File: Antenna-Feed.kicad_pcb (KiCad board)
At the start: 2 copper layers, 74.9 x 97.5 mm, 19 parts, among them J1 Conn_01x01, J10 PC104PTH, J11 PC104PTH, J12 PC104PTH, J13 PC104PTH, J2 B3B-XH-A(LF)(SN), J3 SMA, J4 Conn_01x01, J5 Conn_01x01, J6 Conn_01x01, J7 Conn_01x01, J8 Conn_01x01, J9 B3B-XH-A(LF)(SN), SW1 LIMIT_SWITCH, SW2 LIMIT_SWITCH, U1 B3B-XH-A-AntennaFeed-DC(LF)(S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, U1 B3B-XH-A-AntennaFeed-DepPow(L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, U1 B3B-XH-A-AntennaFeed-RFDep(LF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, U1 NC7SZ157

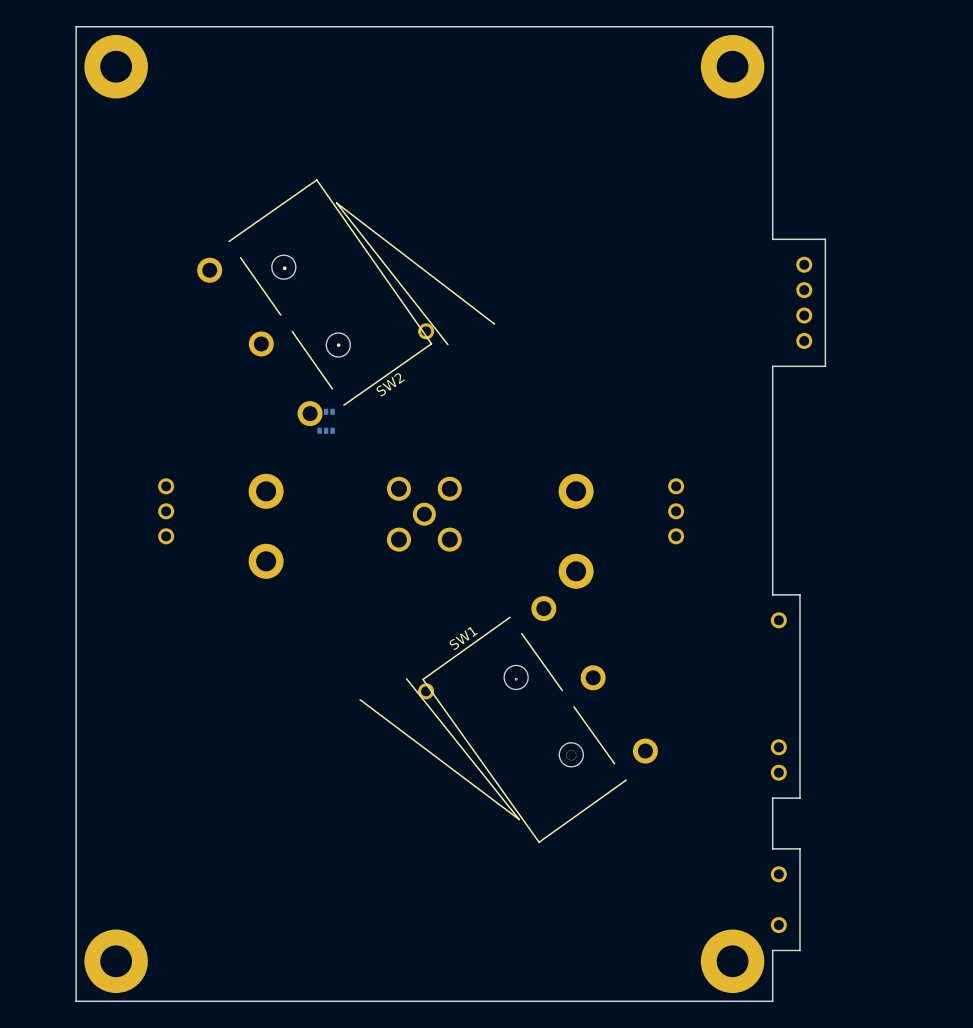
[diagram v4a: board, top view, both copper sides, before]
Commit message: fine tuned component placement
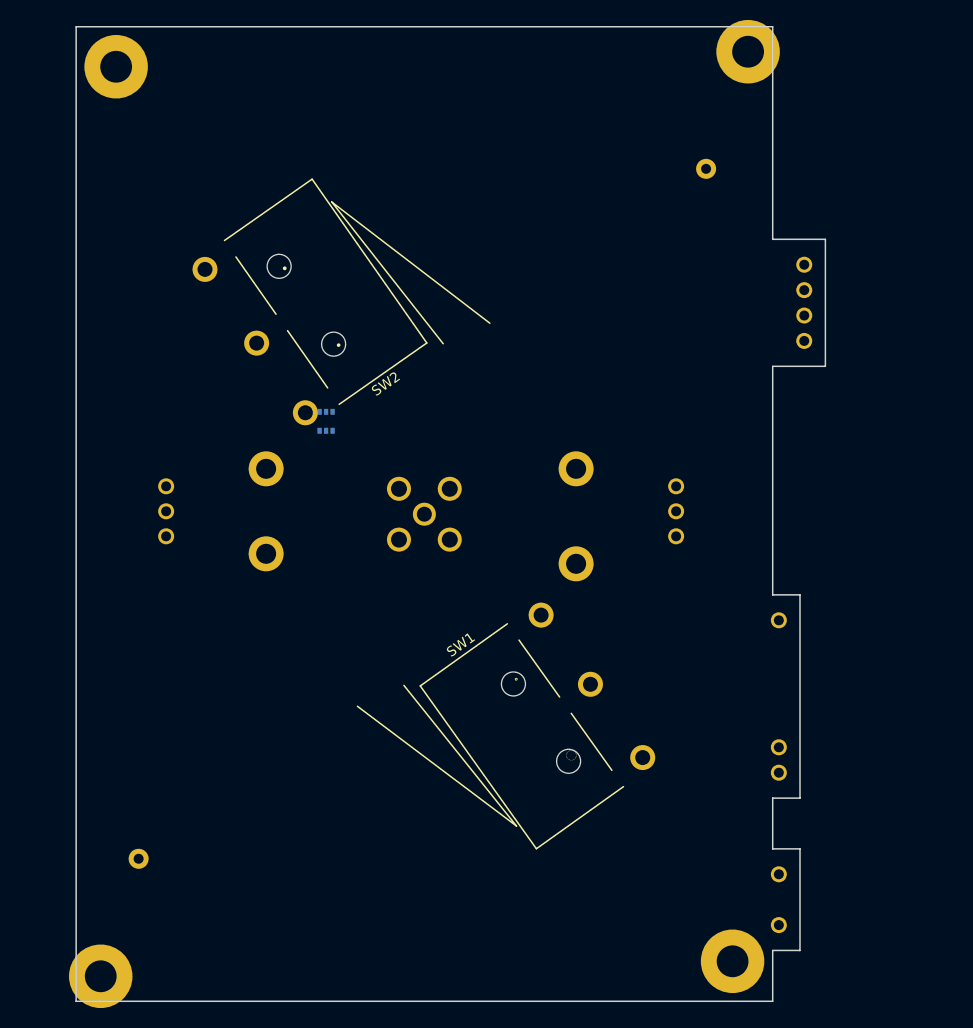
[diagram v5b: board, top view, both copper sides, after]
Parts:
- moved J1 33.3 mm to (96.2, 125.8)
- moved J4 32.4 mm to (153.0, 56.8)
- moved J6 2.25 mm to (109.0, 86.8)
- moved J8 2.25 mm to (140.0, 86.8)
- moved J13 2.16 mm to (157.2, 45.0)
- moved J11 2.15 mm to (92.5, 137.5)
- moved J5 0.75 mm to (109.0, 95.2)
- moved J7 0.75 mm to (140.0, 96.2)
- moved SW1 0.70 mm to (139.7, 109.8)
- moved SW2 0.48 mm to (109.7, 72.7)
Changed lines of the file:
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@@
     (links 17)
     (no_connects 17)
-    (area 89.924999 42.464999 165.005001 140.075001)
+    (area 80.650001 41.755 166.39 144.700001)
     (thickness 1.6)
     (drawings 22)
@@
     (add_net "Net-(J1-Pad1)")
   )
-  (module SFUSat:SMA-Vert-TH (layer B.Cu)
+  (module SFUSat:SMA-Vert-TH locked (layer B.Cu)
     (at 124.825 91.29)
     (fp_text reference J3 (at 0 -5.6) (layer B.SilkS)
@@
     )
   )
-  (module SFUSat:via-0.97mm (layer F.Cu)
-    (at 125 109)
-    (fp_text reference J1 (at 0.0635 2.032) (layer F.SilkS) hide
-      (effects (font (size 1 1) (thickness 0.15)))
-    )
-    (fp_text value Conn_01x01 (at 0.254 -2.8575) (layer F.Fab) hide
-      (effects (font (size 1 1) (thickness 0.15)))
-    )
-    (pad 1 thru_hole circle (at 0 0) (size 1.6 1.6) (drill 1) (layers *.Cu)
-      (net 1 "Net-(J1-Pad1)") (zone_connect 2))
-  )
-  (module SFUSat:via-0.97mm (layer F.Cu)
-    (at 125 73)
-    (fp_text reference J4 (at 0.0635 2.032) (layer F.SilkS) hide
-      (effects (font (size 1 1) (thickness 0.15)))
-    )
-    (fp_text value Conn_01x01 (at 0.254 -2.8575) (layer F.Fab) hide
-      (effects (font (size 1 1) (thickness 0.15)))
-    )
-    (pad 1 thru_hole circle (at 0 0) (size 1.6 1.6) (drill 1) (layers *.Cu)
-      (net 2 "Net-(J3-Pad2)") (zone_connect 2))
-  )
-  (module SFUSat:SS-3GLPD-R (layer F.Cu)
-    (at 140.02 109.16 125.5)
+  (module SFUSat:SS-3GLPD-R locked (layer F.Cu)
+    (at 139.748123 109.810139 125.5)
     (fp_text reference SW1 (at 11 -6 215.5) (layer F.SilkS)
       (effects (font (size 1 1) (thickness 0.15)))
@@
     )
   )
-  (module SFUSat:SS-3GLPD-R (layer F.Cu)
-    (at 110.218904 72.77 305)
+  (module SFUSat:SS-3GLPD-R locked (layer F.Cu)
+    (at 109.748904 72.685278 305)
     (fp_text reference SW2 (at 11 -6 395) (layer F.SilkS)
       (effects (font (size 1 1) (thickness 0.15)))
@@
       (net 8 "Net-(J10-Pad1)"))
   )
-  (module SFUSat:PC104PTH (layer F.Cu)
-    (at 94 136)
+  (module SFUSat:PC104PTH locked (layer F.Cu)
+    (at 92.46 137.5)
     (fp_text reference J11 (at 0 5.08) (layer F.SilkS) hide
       (effects (font (size 1 1) (thickness 0.15)))
@@
       (net 10 "Net-(J12-Pad1)"))
   )
-  (module SFUSat:PC104PTH (layer F.Cu)
-    (at 155.65 46.54)
+  (module SFUSat:PC104PTH locked (layer F.Cu)
+    (at 157.2 45.04)
     (fp_text reference J13 (at 0 5.08) (layer F.SilkS) hide
       (effects (font (size 1 1) (thickness 0.15)))
@@
       (net 11 "Net-(J13-Pad1)"))
   )
-  (module SFUSat:PTH-2.0mm (layer F.Cu)
-    (at 109 96)
+  (module SFUSat:PTH-2.0mm locked (layer F.Cu)
+    (at 109 95.25)
     (fp_text reference J5 (at 0 2.1) (layer F.SilkS) hide
       (effects (font (size 1 1) (thickness 0.15)))
@@
     )
   )
-  (module SFUSat:PTH-2.0mm (layer F.Cu)
-    (at 109 89)
+  (module SFUSat:PTH-2.0mm locked (layer F.Cu)
+    (at 109 86.75)
     (fp_text reference J6 (at 0 2.1) (layer F.SilkS) hide
       (effects (font (size 1 1) (thickness 0.15)))
@@
     )
   )
-  (module SFUSat:PTH-2.0mm (layer F.Cu)
-    (at 140 97)
+  (module SFUSat:PTH-2.0mm locked (layer F.Cu)
+    (at 140 96.25)
     (fp_text reference J7 (at 0 2.1) (layer F.SilkS) hide
       (effects (font (size 1 1) (thickness 0.15)))
@@
     )
   )
-  (module SFUSat:PTH-2.0mm (layer F.Cu)
-    (at 140 89)
+  (module SFUSat:PTH-2.0mm locked (layer F.Cu)
+    (at 140 86.75)
     (fp_text reference J8 (at 0 2.1) (layer F.SilkS) hide
       (effects (font (size 1 1) (thickness 0.15)))
@@
     (pad 26A thru_hole circle (at 5.08 0 90) (size 1.6 1.6) (drill 1) (layers *.Cu *.Mask))
   )
+  (module SFUSat:via-0.97mm locked (layer F.Cu)
+    (at 153 56.75)
+    (fp_text reference J4 (at 0.0635 2.032) (layer F.SilkS) hide
+      (effects (font (size 1 1) (thickness 0.15)))
+    )
+    (fp_text value Conn_01x01 (at 0.254 -2.8575) (layer F.Fab) hide
+      (effects (font (size 1 1) (thickness 0.15)))
+    )
+    (pad 1 thru_hole circle (at 0 0) (size 2 2) (drill 1) (layers *.Cu *.Mask)
+      (net 2 "Net-(J3-Pad2)") (zone_connect 2))
+  )
+  (module SFUSat:via-0.97mm locked (layer F.Cu)
+    (at 96.25 125.75)
+    (fp_text reference J1 (at 0.0635 2.032) (layer F.SilkS) hide
+      (effects (font (size 1 1) (thickness 0.15)))
+    )
+    (fp_text value Conn_01x01 (at 0.254 -2.8575) (layer F.Fab) hide
+      (effects (font (size 1 1) (thickness 0.15)))
+    )
+    (pad 1 thru_hole circle (at 0 0) (size 2 2) (drill 1) (layers *.Cu *.Mask)
+      (net 1 "Net-(J1-Pad1)") (zone_connect 2))
+  )
   (gr_circle (center 116.25 74.38) (end 116.33 74.38) (layer F.SilkS) (width 0.2))

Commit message: Fixed alignment of side connector pins. Added connector pins to left side.
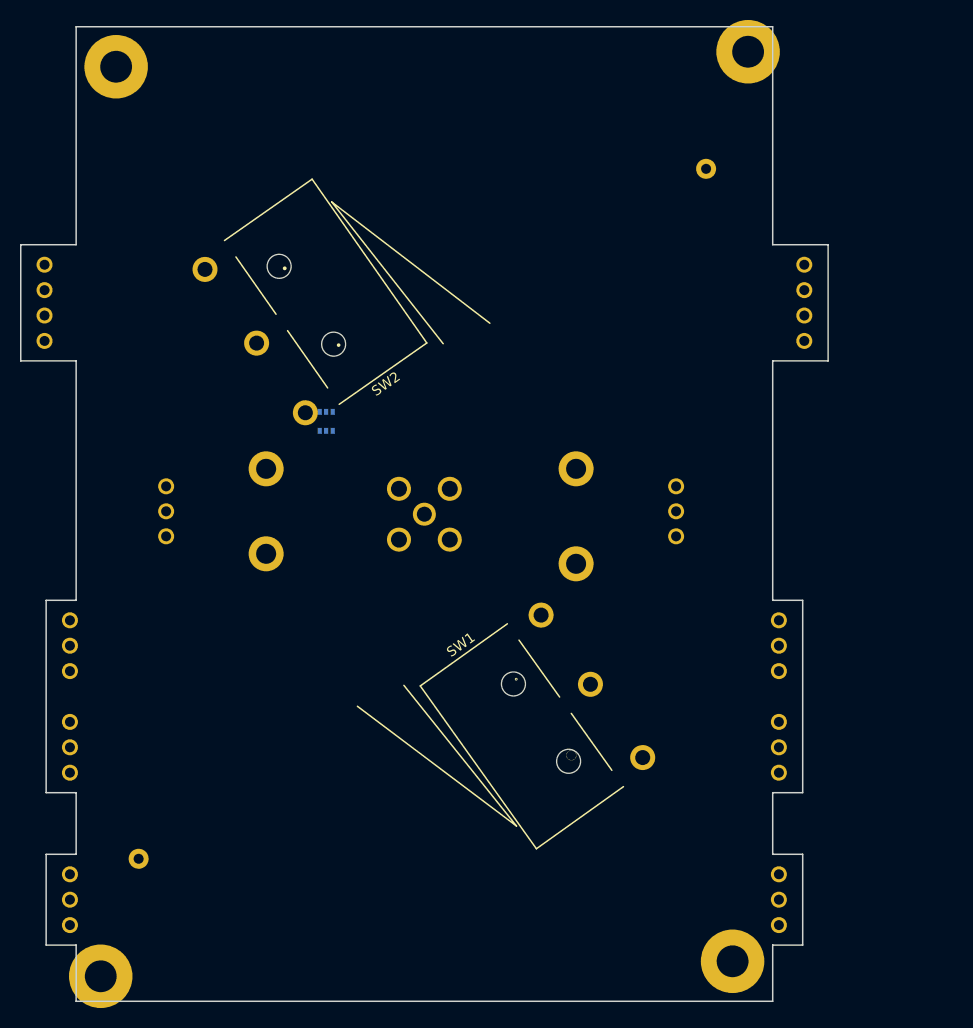
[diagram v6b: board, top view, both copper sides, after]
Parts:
- removed the U1 at (160.3, 132.4)
- removed the U1 at (160.3, 117.1)
- removed the U1 at (162.8, 74.0)
- added U1: B3B-XH-A-AntennaFeed-DepPow(LF)(SN), SFUSat:B3B-XH-A-AntennaFeed-DepPow, B.Cu at (86.8, 74.0)
- added U1: B3B-XH-A-AntennaFeed-DepPow(LF)(SN), SFUSat:B3B-XH-A-AntennaFeed-DepPow, B.Cu at (162.8, 74.0)
- added U1: B3B-XH-A-AntennaFeed-RFDep(LF)(SN), SFUSat:B3B-XH-A-AntennaFeed-RFDep, B.Cu at (89.4, 117.1)
- added U1: B3B-XH-A-AntennaFeed-RFDep(LF)(SN), SFUSat:B3B-XH-A-AntennaFeed-RFDep, B.Cu at (160.3, 117.1)
- added U1: B3B-XH-A-AntennaFeed-DC(LF)(SN), SFUSat:B3B-XH-A-AntennaFeed-DC, B.Cu at (160.3, 132.4)
- added U1: B3B-XH-A-AntennaFeed-DC(LF)(SN), SFUSat:B3B-XH-A-AntennaFeed-DC, B.Cu at (89.4, 132.4)
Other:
- board size 74.9 x 97.5 mm -> 80.7 x 97.5 mm

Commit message: Added new connectors to PCB and removed the old connectors from the left side.
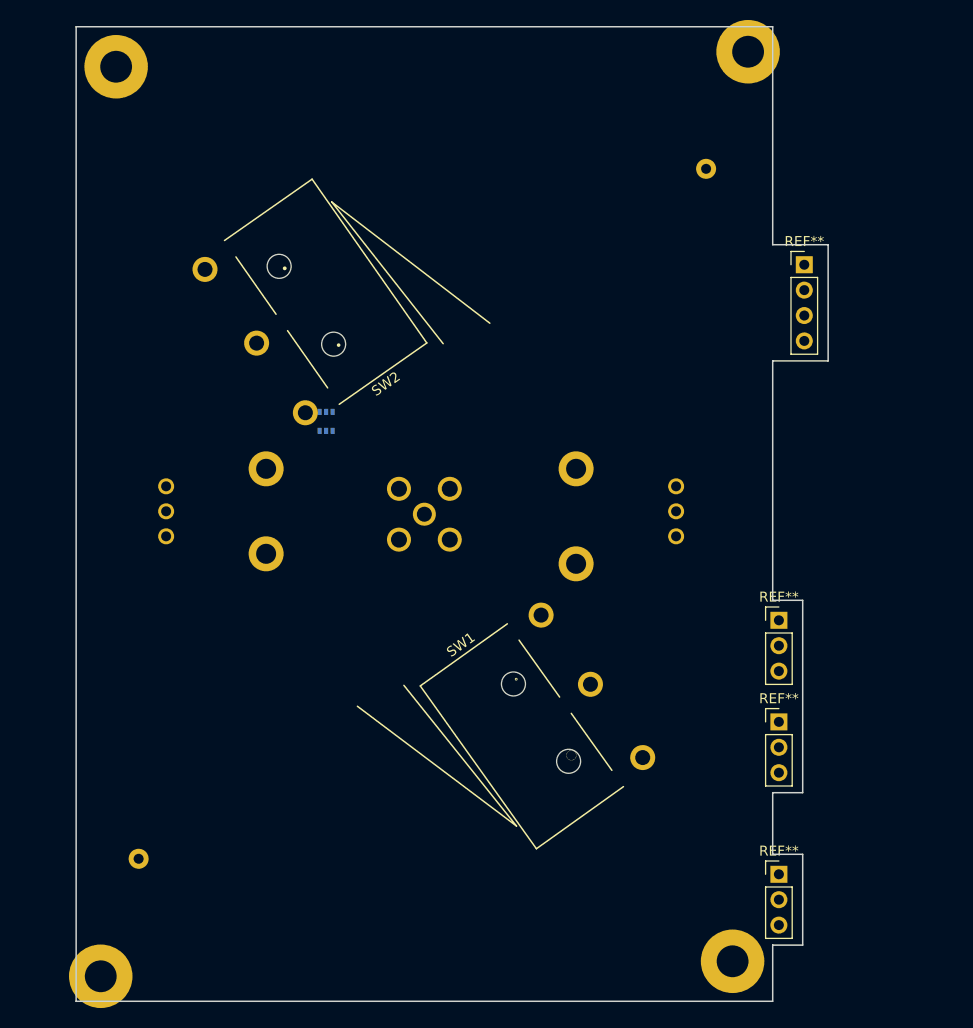
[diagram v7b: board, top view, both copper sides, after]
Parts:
- removed the U1 at (86.8, 74.0)
- removed the U1 at (162.8, 74.0)
- removed the U1 at (89.4, 117.1)
- removed the U1 at (160.3, 117.1)
- removed the U1 at (160.3, 132.4)
- removed the U1 at (89.4, 132.4)
- added REF**: Socket_Strip_Straight_1x03_Pitch2.54mm, Socket_Strips:Socket_Strip_Straight_1x03_Pitch2.54mm, F.Cu at (160.3, 112.1)
- added REF**: Socket_Strip_Straight_1x03_Pitch2.54mm, Socket_Strips:Socket_Strip_Straight_1x03_Pitch2.54mm, F.Cu at (160.3, 101.9)
- added REF**: Socket_Strip_Straight_1x03_Pitch2.54mm, Socket_Strips:Socket_Strip_Straight_1x03_Pitch2.54mm, F.Cu at (160.3, 127.3)
- added REF**: Socket_Strip_Straight_1x04_Pitch2.54mm, Socket_Strips:Socket_Strip_Straight_1x04_Pitch2.54mm, F.Cu at (162.8, 66.3)
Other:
- board size 80.7 x 97.5 mm -> 75.2 x 97.5 mm

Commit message: design complete
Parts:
- removed J9: B3B-XH-A(LF)(SN), SFUSat:B3B-XH-A
- removed REF** (x3): Socket_Strip_Straight_1x03_Pitch2.54mm, Socket_Strips:Socket_Strip_Straight_1x03_Pitch2.54mm
- removed REF**: Socket_Strip_Straight_1x04_Pitch2.54mm, Socket_Strips:Socket_Strip_Straight_1x04_Pitch2.54mm
- added J16: Conn_01x03, Socket_Strips:Socket_Strip_Straight_1x03_Pitch2.54mm, F.Cu at (153.0, 74.0)
- added J17: Conn_01x03, Socket_Strips:Socket_Strip_Straight_1x03_Pitch2.54mm, F.Cu at (152.8, 118.5)
- added U2: NC7SZ157, SFUSat:SOT-363, B.Cu at (148.5, 101.8)
- J2: value B3B-XH-A(LF)(SN) -> PC104-8BIT; footprint SFUSat:B3B-XH-A -> SFUSat:PC104-8bit; moved to F.Cu
- U1: moved to F.Cu
- moved J2 62.6 mm to (161.5, 93.0), turned to 0 degrees
- moved U1 40.5 mm to (148.5, 104.8), turned to 270 degrees
- moved J7 9.50 mm to (140.0, 86.8)
- moved J8 9.50 mm to (140.0, 96.2)
- moved J5 8.50 mm to (109.0, 86.8)
- moved J6 8.50 mm to (109.0, 95.2)
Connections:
- net Net-(SW1-PadNC) renamed /MUX/IN0
- net Net-(SW2-PadNC) renamed /MUX/IN1
- J5 pad 1: Net-(J2-Pad1) -> /GNDPWR
- J6 pad 1: GND -> Net-(J6-Pad1)
- J7 pad 1: GND -> Net-(J6-Pad1)
- J8 pad 1: Net-(J2-Pad2) -> Net-(J16-Pad2)
- SW1 pad COM: Net-(J9-Pad1) -> /3V3
- SW2 pad COM: Net-(J9-Pad1) -> /3V3
- U1 pad 4: Net-(J9-Pad2) -> /MUX/OUT
- U1 pad 5: Net-(J9-Pad1) -> /3V3
- U1 pad 6: Net-(J9-Pad3) -> /RF.DEPLOY2
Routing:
- net /3V3: track 0.00 -> 115.1 mm, vias 0 -> 1
- net /MUX/IN1: track 0.00 -> 66.1 mm, vias 0 -> 1
- net /GNDPWR: track 0.00 -> 64.1 mm
- net Net-(J1-Pad1): track 0.00 -> 46.3 mm
- net GND: track 0.00 -> 43.8 mm, vias 0 -> 2
- net Net-(J3-Pad2): track 0.00 -> 41.0 mm
- net Net-(J6-Pad1): track 0.00 -> 37.6 mm
- net Net-(J16-Pad2): track 0.00 -> 34.0 mm
- net /MUX/IN0: track 0.00 -> 24.7 mm
- net /MUX/OUT: track 0.00 -> 19.6 mm, vias 0 -> 1
- net /RF.DEPLOY2: track 0.00 -> 13.2 mm, vias 0 -> 1
- net /RF.DEPLOY0: track 0.00 -> 8.09 mm
- net /RF.DEPLOY1: track 0.00 -> 7.98 mm
- added copper zone on F.Cu, net /DEPLOY.+Z
- added copper zone on F.Cu, net /DEPLOY.-Z
- added copper zone on B.Cu, net /GNDPWR
- added copper zone on F.Cu, net Net-(J3-Pad2)
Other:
- board size 75.2 x 97.5 mm -> 75 x 97.5 mm
- net class Default: clearance 0.2 -> 0.1524
- rule pad_to_mask_clearance: 0.2 -> 0.025
- rule trace_clearance: 0.2 -> 0.1524
- rule trace_min: 0.2 -> 0.1524
